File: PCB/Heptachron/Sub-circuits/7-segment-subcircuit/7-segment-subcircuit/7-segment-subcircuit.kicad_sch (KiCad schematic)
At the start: 7 parts

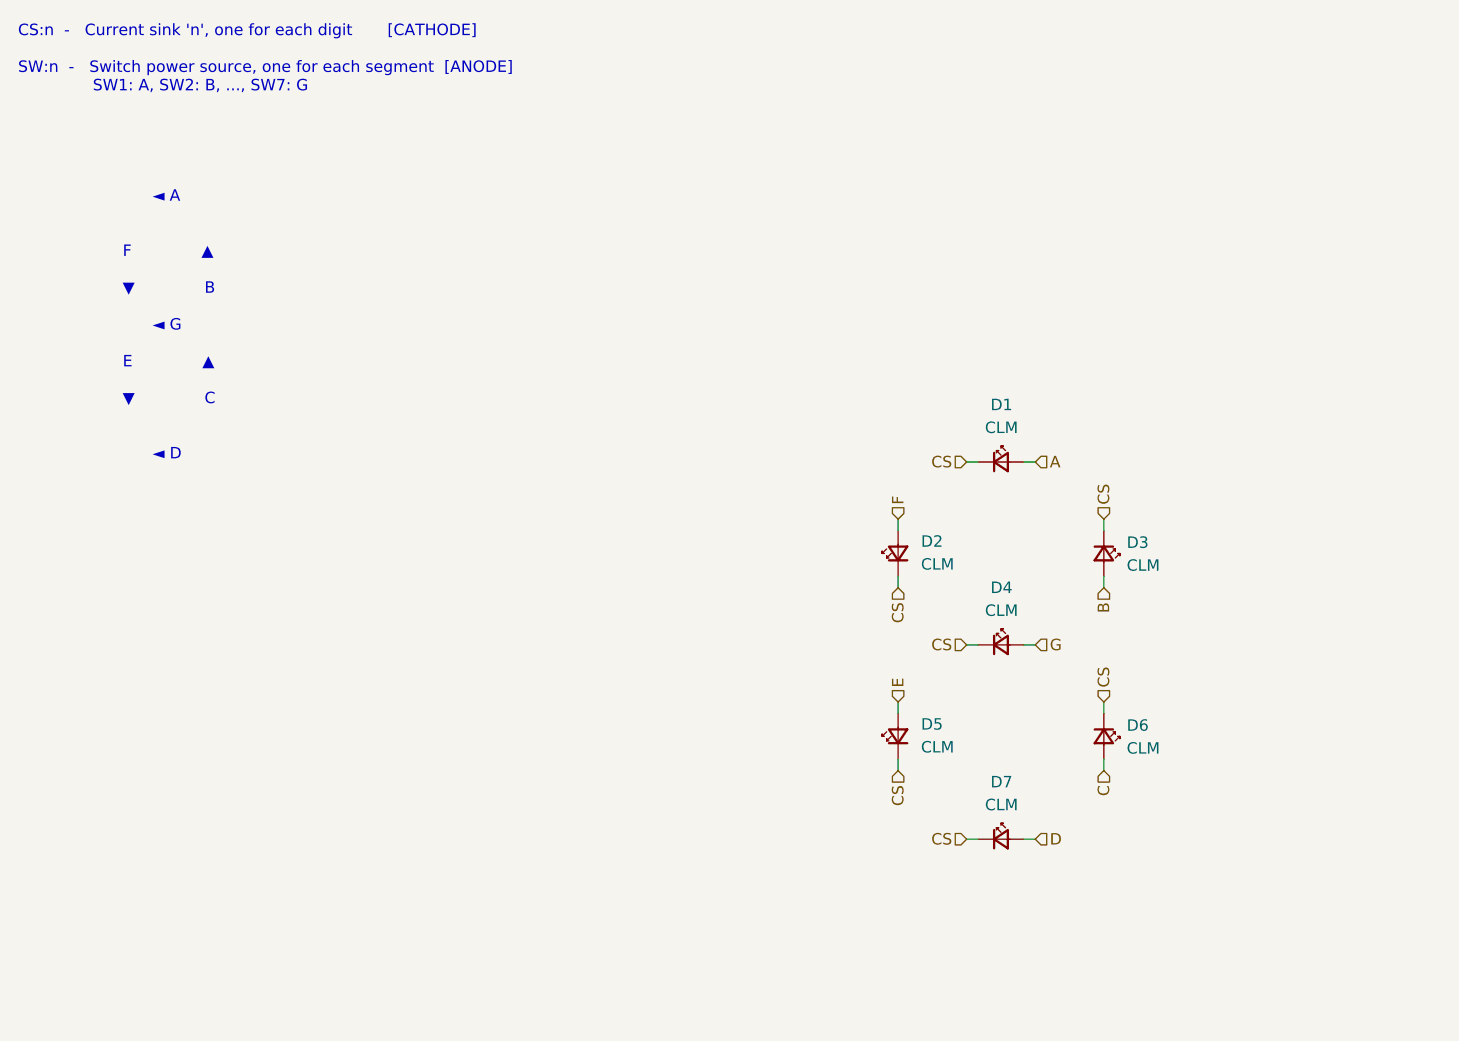
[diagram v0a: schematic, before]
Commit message: Continue schematic, symbols & footprints for digits
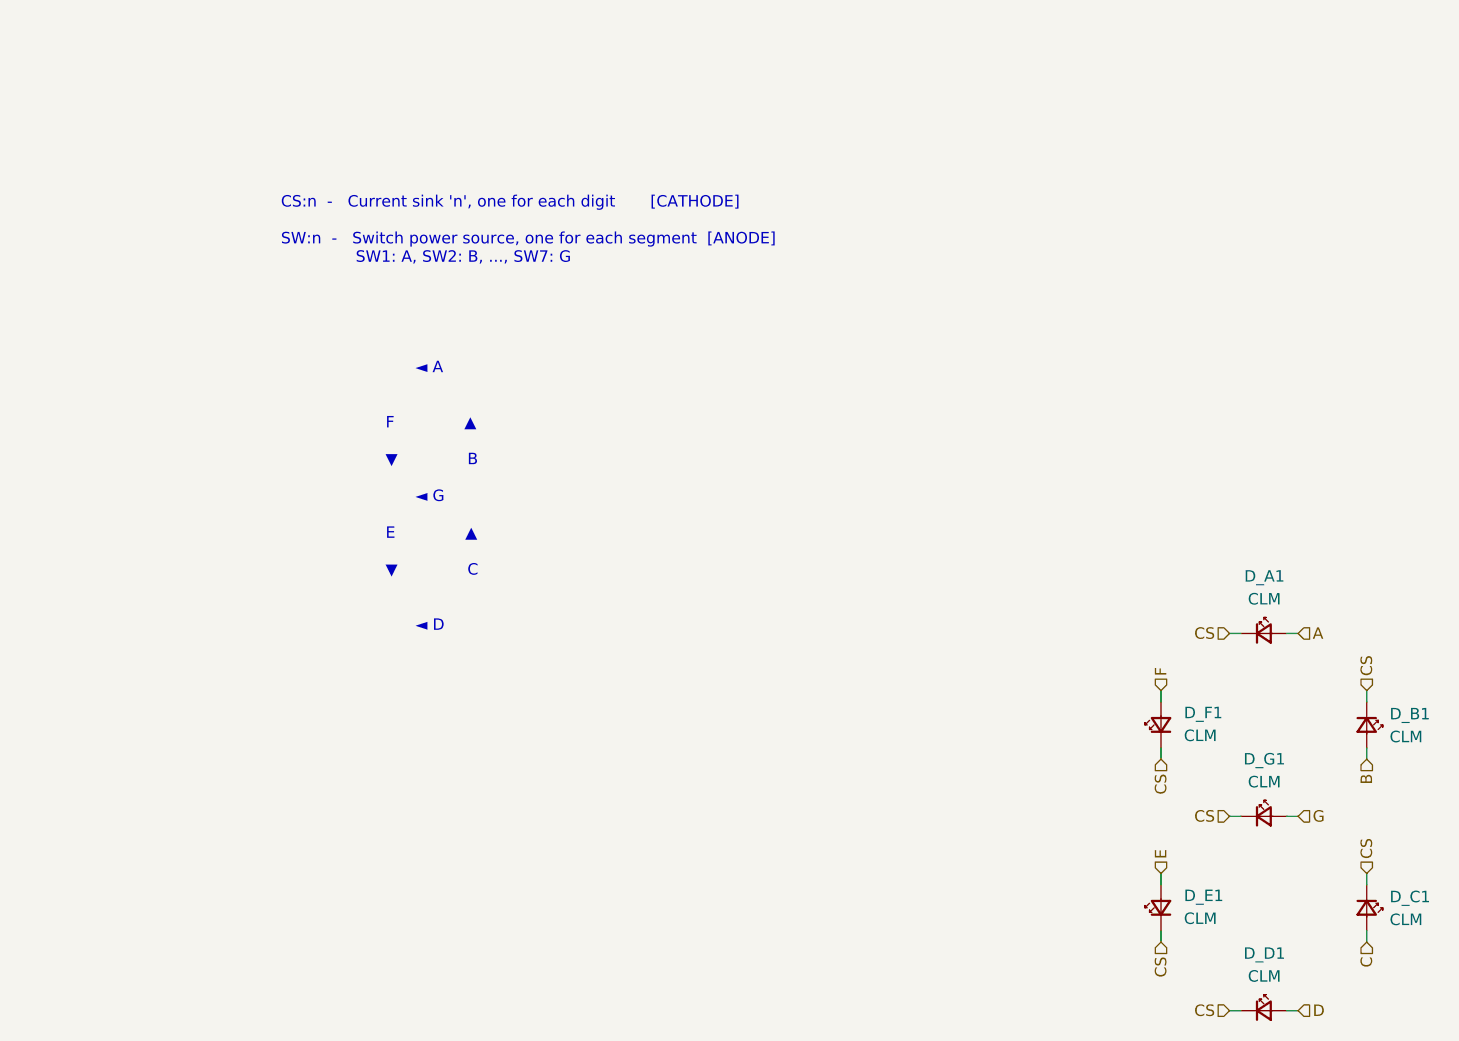
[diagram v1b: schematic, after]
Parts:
- removed D1, D2, D3, D4, D5, D6, D7: CLM, Heptachron-Lib:CREE-PLCC2-angled, symbol Device:LED_Small
- added D_A1, D_B1, D_C1, D_D1, D_E1, D_F1, D_G1: CLM, Heptachron-Lib:CREE-PLCC2-angled, symbol Device:LED_Small
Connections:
- net A: now also D_A1.2 (A)
- net B: now also D_B1.2 (A)
- net C: now also D_C1.2 (A)
- net CS: now also D_A1.1 (K), D_B1.1 (K), D_C1.1 (K), D_D1.1 (K), D_E1.1 (K), D_F1.1 (K), D_G1.1 (K)
- net D: now also D_D1.2 (A)
- net E: now also D_E1.2 (A)
- net F: now also D_F1.2 (A)
- net G: now also D_G1.2 (A)
